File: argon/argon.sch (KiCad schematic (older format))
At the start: 72 parts, among them J1 USB, J2 V3V3-GND, J3 V3V3-GND, J4 V3V3-GND, J5 V3V3-GND, U1 LMC555xM, U2 AMS1117-3.3, U3 93LCxxA, U4 LMC555xM, U5 FT2232HL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

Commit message: Argon PCB - part 2 + logo
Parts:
- C17, C6: value 1uF -> 100nF
- H1, H2, H3, H4: footprint (none) -> MountingHole:MountingHole_3.2mm_M3
- R15, R3: value 100K -> 1M
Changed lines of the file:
@@
 	3800 10400 3650 10400
 Wire Wire Line
-	5000 10400 5000 10550
+	5050 10400 5050 10550
 $Comp
 L power:GND #PWR012
 U 1 1 5FD2B388
-P 5000 10550
-F 0 "#PWR012" H 5000 10300 50  0001 C CNN
-F 1 "GND" H 5005 10377 50  0000 C CNN
-F 2 "" H 5000 10550 50  0001 C CNN
-F 3 "" H 5000 10550 50  0001 C CNN
-	1    5000 10550
+P 5050 10550
+F 0 "#PWR012" H 5050 10300 50  0001 C CNN
+F 1 "GND" H 5055 10377 50  0000 C CNN
+F 2 "" H 5050 10550 50  0001 C CNN
+F 3 "" H 5050 10550 50  0001 C CNN
+	1    5050 10550
 	1    0    0    -1
 $EndComp
@@
 P 4700 10400
 F 0 "C6" V 4750 10250 50  0000 C CNN
-F 1 "1uF" V 4650 10250 50  0000 C CNN
+F 1 "100nF" V 4650 10200 50  0000 C CNN
 F 2 "Capacitor_SMD:C_0603_1608Metric" H 4700 10400 50  0001 C CNN
 F 3 "~" H 4700 10400 50  0001 C CNN
@@
 	4300 10400 4100 10400
 Wire Wire Line
-	4850 10400 5000 10400
+	4850 10400 5050 10400
 Wire Wire Line
 	2750 9850 2300 9850
@@
 P 3950 10400
 F 0 "R3" V 4050 10400 50  0000 C CNN
-F 1 "100K" V 3850 10400 50  0000 C CNN
+F 1 "1M" V 3850 10400 50  0000 C CNN
 F 2 "Resistor_SMD:R_0603_1608Metric" V 3880 10400 50  0001 C CNN
 F 3 "~" H 3950 10400 50  0001 C CNN
@@
 	8000 10400 7850 10400
 Wire Wire Line
-	9200 10400 9200 10550
+	9250 10400 9250 10550
 $Comp
 L power:GND #PWR024
 U 1 1 60E50CB0
-P 9200 10550
-F 0 "#PWR024" H 9200 10300 50  0001 C CNN
-F 1 "GND" H 9205 10377 50  0000 C CNN
-F 2 "" H 9200 10550 50  0001 C CNN
-F 3 "" H 9200 10550 50  0001 C CNN
-	1    9200 10550
+P 9250 10550
+F 0 "#PWR024" H 9250 10300 50  0001 C CNN
+F 1 "GND" H 9255 10377 50  0000 C CNN
+F 2 "" H 9250 10550 50  0001 C CNN
+F 3 "" H 9250 10550 50  0001 C CNN
+	1    9250 10550
 	1    0    0    -1
 $EndComp
@@
 P 8900 10400
 F 0 "C17" V 8950 10250 50  0000 C CNN
-F 1 "1uF" V 8850 10250 50  0000 C CNN
+F 1 "100nF" V 8850 10200 50  0000 C CNN
 F 2 "Capacitor_SMD:C_0603_1608Metric" H 8900 10400 50  0001 C CNN
 F 3 "~" H 8900 10400 50  0001 C CNN
@@
 	8500 10400 8300 10400
 Wire Wire Line
-	9050 10400 9200 10400
+	9050 10400 9250 10400
 Wire Wire Line
 	6950 9850 6500 9850
@@
 P 8150 10400
 F 0 "R15" V 8250 10400 50  0000 C CNN
-F 1 "100K" V 8050 10400 50  0000 C CNN
+F 1 "1M" V 8050 10400 50  0000 C CNN
 F 2 "Resistor_SMD:R_0603_1608Metric" V 8080 10400 50  0001 C CNN
 F 3 "~" H 8150 10400 50  0001 C CNN
@@
 F 0 "H1" H 15150 8096 50  0000 L CNN
 F 1 "MountingHole" H 15150 8005 50  0000 L CNN
-F 2 "" H 15050 8050 50  0001 C CNN
+F 2 "MountingHole:MountingHole_3.2mm_M3" H 15050 8050 50  0001 C CNN
 F 3 "~" H 15050 8050 50  0001 C CNN
 	1    15050 8050
@@
 F 0 "H2" H 15150 8346 50  0000 L CNN
 F 1 "MountingHole" H 15150 8255 50  0000 L CNN
-F 2 "" H 15050 8300 50  0001 C CNN
+F 2 "MountingHole:MountingHole_3.2mm_M3" H 15050 8300 50  0001 C CNN
 F 3 "~" H 15050 8300 50  0001 C CNN
 	1    15050 8300
@@
 F 0 "H3" H 15150 8596 50  0000 L CNN
 F 1 "MountingHole" H 15150 8505 50  0000 L CNN
-F 2 "" H 15050 8550 50  0001 C CNN
+F 2 "MountingHole:MountingHole_3.2mm_M3" H 15050 8550 50  0001 C CNN
 F 3 "~" H 15050 8550 50  0001 C CNN
 	1    15050 8550
@@
 F 0 "H4" H 15150 8846 50  0000 L CNN
 F 1 "MountingHole" H 15150 8755 50  0000 L CNN
-F 2 "" H 15050 8800 50  0001 C CNN
+F 2 "MountingHole:MountingHole_3.2mm_M3" H 15050 8800 50  0001 C CNN
 F 3 "~" H 15050 8800 50  0001 C CNN
 	1    15050 8800

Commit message: Change some capacitors to tantals
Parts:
- C12, C13, C7: footprint Capacitor_SMD:C_0603_1608Metric -> Capacitor_Tantalum_SMD:CP_EIA-3216-18_Kemet-A
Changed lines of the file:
@@
 F 0 "C7" H 5850 4500 50  0000 C CNN
 F 1 "4.7uF" H 5900 4300 50  0000 C CNN
-F 2 "Capacitor_SMD:C_0603_1608Metric" H 5750 4400 50  0001 C CNN
+F 2 "Capacitor_Tantalum_SMD:CP_EIA-3216-18_Kemet-A" H 5750 4400 50  0001 C CNN
 F 3 "~" H 5750 4400 50  0001 C CNN
 	1    5750 4400
@@
 F 0 "C12" H 7150 1650 50  0000 C CNN
 F 1 "4.7uF" H 7200 1450 50  0000 C CNN
-F 2 "Capacitor_SMD:C_0603_1608Metric" H 7050 1550 50  0001 C CNN
+F 2 "Capacitor_Tantalum_SMD:CP_EIA-3216-18_Kemet-A" H 7050 1550 50  0001 C CNN
 F 3 "~" H 7050 1550 50  0001 C CNN
 	1    7050 1550
@@
 F 0 "C13" H 7150 2650 50  0000 C CNN
 F 1 "4.7uF" H 7200 2450 50  0000 C CNN
-F 2 "Capacitor_SMD:C_0603_1608Metric" H 7050 2550 50  0001 C CNN
+F 2 "Capacitor_Tantalum_SMD:CP_EIA-3216-18_Kemet-A" H 7050 2550 50  0001 C CNN
 F 3 "~" H 7050 2550 50  0001 C CNN
 	1    7050 2550

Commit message: PCB - chaotic
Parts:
- D1, D2, D3, D4, D5, D6, D7: footprint LED_SMD:LED_0805_2012Metric -> benzene:LED_0805_2012Metric
- U1, U4: footprint Package_SO:SOIC-8_3.9x4.9mm_P1.27mm -> Package_SO:VSSOP-8_3.0x3.0mm_P0.65mm
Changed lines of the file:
@@
 F 0 "D1" H 4650 9550 50  0000 C CNN
 F 1 "LED" H 4650 9750 50  0000 C CNN
-F 2 "LED_SMD:LED_0805_2012Metric" H 4650 9650 50  0001 C CNN
+F 2 "benzene:LED_0805_2012Metric" H 4650 9650 50  0001 C CNN
 F 3 "~" H 4650 9650 50  0001 C CNN
 	1    4650 9650
@@
 F 0 "U1" H 3550 10200 50  0000 C CNN
 F 1 "LMC555xM" H 3500 9500 50  0000 C CNN
-F 2 "Package_SO:SOIC-8_3.9x4.9mm_P1.27mm" H 4100 9450 50  0001 C CNN
+F 2 "Package_SO:VSSOP-8_3.0x3.0mm_P0.65mm" H 4100 9450 50  0001 C CNN
 F 3 "http://www.ti.com/lit/ds/symlink/lmc555.pdf" H 4100 9450 50  0001 C CNN
 	1    3250 9850
@@
 F 0 "D4" H 14350 1150 50  0000 C CNN
 F 1 "LED" H 14350 1400 50  0000 C CNN
-F 2 "LED_SMD:LED_0805_2012Metric" H 14350 1250 50  0001 C CNN
+F 2 "benzene:LED_0805_2012Metric" H 14350 1250 50  0001 C CNN
 F 3 "~" H 14350 1250 50  0001 C CNN
 	1    14350 1250
@@
 F 0 "D5" H 14350 1550 50  0000 C CNN
 F 1 "LED" H 14350 1800 50  0000 C CNN
-F 2 "LED_SMD:LED_0805_2012Metric" H 14350 1650 50  0001 C CNN
+F 2 "benzene:LED_0805_2012Metric" H 14350 1650 50  0001 C CNN
 F 3 "~" H 14350 1650 50  0001 C CNN
 	1    14350 1650
@@
 F 0 "D6" H 14350 1950 50  0000 C CNN
 F 1 "LED" H 14350 2200 50  0000 C CNN
-F 2 "LED_SMD:LED_0805_2012Metric" H 14350 2050 50  0001 C CNN
+F 2 "benzene:LED_0805_2012Metric" H 14350 2050 50  0001 C CNN
 F 3 "~" H 14350 2050 50  0001 C CNN
 	1    14350 2050
@@
 F 0 "D7" H 14350 2350 50  0000 C CNN
 F 1 "LED" H 14350 2600 50  0000 C CNN
-F 2 "LED_SMD:LED_0805_2012Metric" H 14350 2450 50  0001 C CNN
+F 2 "benzene:LED_0805_2012Metric" H 14350 2450 50  0001 C CNN
 F 3 "~" H 14350 2450 50  0001 C CNN
 	1    14350 2450
@@
 F 0 "D3" H 8850 9550 50  0000 C CNN
 F 1 "LED" H 8850 9750 50  0000 C CNN
-F 2 "LED_SMD:LED_0805_2012Metric" H 8850 9650 50  0001 C CNN
+F 2 "benzene:LED_0805_2012Metric" H 8850 9650 50  0001 C CNN
 F 3 "~" H 8850 9650 50  0001 C CNN
 	1    8850 9650
@@
 F 0 "U4" H 7750 10200 50  0000 C CNN
 F 1 "LMC555xM" H 7700 9500 50  0000 C CNN
-F 2 "Package_SO:SOIC-8_3.9x4.9mm_P1.27mm" H 8300 9450 50  0001 C CNN
+F 2 "Package_SO:VSSOP-8_3.0x3.0mm_P0.65mm" H 8300 9450 50  0001 C CNN
 F 3 "http://www.ti.com/lit/ds/symlink/lmc555.pdf" H 8300 9450 50  0001 C CNN
 	1    7450 9850
@@
 F 0 "D2" H 5950 3050 50  0000 C CNN
 F 1 "LED" H 5950 3300 50  0000 C CNN
-F 2 "LED_SMD:LED_0805_2012Metric" H 5950 3150 50  0001 C CNN
+F 2 "benzene:LED_0805_2012Metric" H 5950 3150 50  0001 C CNN
 F 3 "~" H 5950 3150 50  0001 C CNN
 	1    5950 3150

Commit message: Piotrek's review
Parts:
- removed C5: 22uF, Capacitor_SMD:C_0603_1608Metric, symbol Device:C
- added C25, C5: 22uF, Capacitor_Tantalum_SMD:CP_EIA-3216-18_Kemet-A, symbol Device:CP1
- added U6: USBLC6-2SC6, Package_TO_SOT_SMD:SOT-23-6, symbol Power_Protection:USBLC6-2SC6
- C17, C6: symbol Device:CP1 -> Device:C
- C3, C9: value 10uF -> 10nF
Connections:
- net GND: now also C25.2, C5.2, U6.2 (GND)
- net V3V3: now also C5.1
- net VBUS: now reaches C4.1, J1.1 (VBUS), U2.3 (VI)
- net VBUS: now also C25.1, U6.5 (VBUS)
- net at J1.2 (D-): now also U6.1 (I/O1); no longer R12.2
- net at J1.3 (D+): now also U6.3 (I/O2); no longer R13.2
- new net: R12.2, U6.6 (I/O1)
- new net: R13.2, U6.4 (I/O2)
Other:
- moved on the sheet: C1, C2, C4, J1, R2, U2

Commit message: Argon - all elements and start paths
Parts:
- added J6, J7: V3V3-GND, Connector_PinHeader_2.54mm:PinHeader_1x02_P2.54mm_Vertical, symbol ArgonComponents:V3V3-GND
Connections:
- net GND: now also J6.1 (GND), J7.1 (GND)
- net V3V3: now also J6.2 (V3V3), J7.2 (V3V3)
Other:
- moved on the sheet: J2, J3, J4, J5
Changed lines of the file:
@@
 L ArgonComponents:V3V3-GND J2
 U 1 1 5FE8C355
-P 11550 8000
-F 0 "J2" H 11467 7777 50  0000 C CNN
-F 1 "V3V3-GND" H 11550 7800 50  0001 C CNN
-F 2 "Connector_PinHeader_2.54mm:PinHeader_1x02_P2.54mm_Vertical" H 11550 8000 50  0001 C CNN
-F 3 "~" H 11550 8000 50  0001 C CNN
-	1    11550 8000
-	-1   0    0    1
-$EndComp
-Wire Wire Line
-	11850 8000 12050 8000
-Wire Wire Line
-	12050 8000 12050 8100
-Wire Wire Line
-	11850 7900 12050 7900
+P 11550 7700
+F 0 "J2" H 11467 7477 50  0000 C CNN
+F 1 "V3V3-GND" H 11550 7500 50  0001 C CNN
+F 2 "Connector_PinHeader_2.54mm:PinHeader_1x02_P2.54mm_Vertical" H 11550 7700 50  0001 C CNN
+F 3 "~" H 11550 7700 50  0001 C CNN
+	1    11550 7700
+	-1   0    0    1
+$EndComp
+Wire Wire Line
+	11850 7700 12050 7700
+Wire Wire Line
+	12050 7700 12050 7800
+Wire Wire Line
+	11850 7600 12050 7600
 $Comp
 L power:GND #PWR027
 U 1 1 5FEAE107
-P 12050 8100
-F 0 "#PWR027" H 12050 7850 50  0001 C CNN
-F 1 "GND" H 12055 7927 50  0000 C CNN
-F 2 "" H 12050 8100 50  0001 C CNN
-F 3 "" H 12050 8100 50  0001 C CNN
-	1    12050 8100
-	1    0    0    -1
-$EndComp
-Text GLabel 12050 7900 2    50   Input ~ 0
+P 12050 7800
+F 0 "#PWR027" H 12050 7550 50  0001 C CNN
+F 1 "GND" H 12055 7627 50  0000 C CNN
+F 2 "" H 12050 7800 50  0001 C CNN
+F 3 "" H 12050 7800 50  0001 C CNN
+	1    12050 7800
+	1    0    0    -1
+$EndComp
+Text GLabel 12050 7600 2    50   Input ~ 0
 V3V3
 NoConn ~ 9750 7300
@@
 L ArgonComponents:V3V3-GND J3
 U 1 1 610EB3FD
-P 11550 8800
-F 0 "J3" H 11467 8577 50  0000 C CNN
-F 1 "V3V3-GND" H 11550 8600 50  0001 C CNN
-F 2 "Connector_PinHeader_2.54mm:PinHeader_1x02_P2.54mm_Vertical" H 11550 8800 50  0001 C CNN
-F 3 "~" H 11550 8800 50  0001 C CNN
-	1    11550 8800
-	-1   0    0    1
-$EndComp
-Wire Wire Line
-	11850 8800 12050 8800
-Wire Wire Line
-	12050 8800 12050 8900
-Wire Wire Line
-	11850 8700 12050 8700
+P 11550 8500
+F 0 "J3" H 11467 8277 50  0000 C CNN
+F 1 "V3V3-GND" H 11550 8300 50  0001 C CNN
+F 2 "Connector_PinHeader_2.54mm:PinHeader_1x02_P2.54mm_Vertical" H 11550 8500 50  0001 C CNN
+F 3 "~" H 11550 8500 50  0001 C CNN
+	1    11550 8500
+	-1   0    0    1
+$EndComp
+Wire Wire Line
+	11850 8500 12050 8500
+Wire Wire Line
+	12050 8500 12050 8600
+Wire Wire Line
+	11850 8400 12050 8400
 $Comp
 L power:GND #PWR0101
 U 1 1 610EB406
-P 12050 8900
-F 0 "#PWR0101" H 12050 8650 50  0001 C CNN
-F 1 "GND" H 12055 8727 50  0000 C CNN
-F 2 "" H 12050 8900 50  0001 C CNN
-F 3 "" H 12050 8900 50  0001 C CNN
-	1    12050 8900
-	1    0    0    -1
-$EndComp
-Text GLabel 12050 8700 2    50   Input ~ 0
+P 12050 8600
+F 0 "#PWR0101" H 12050 8350 50  0001 C CNN
+F 1 "GND" H 12055 8427 50  0000 C CNN
+F 2 "" H 12050 8600 50  0001 C CNN
+F 3 "" H 12050 8600 50  0001 C CNN
+	1    12050 8600
+	1    0    0    -1
+$EndComp
+Text GLabel 12050 8400 2    50   Input ~ 0
 V3V3
 $Comp
@@
 L ArgonComponents:V3V3-GND J4
 U 1 1 61468AEA
-P 13050 8000
-F 0 "J4" H 12967 7777 50  0000 C CNN
-F 1 "V3V3-GND" H 13050 7800 50  0001 C CNN
-F 2 "Connector_PinHeader_2.54mm:PinHeader_1x02_P2.54mm_Vertical" H 13050 8000 50  0001 C CNN
-F 3 "~" H 13050 8000 50  0001 C CNN
-	1    13050 8000
-	-1   0    0    1
-$EndComp
-Wire Wire Line
-	13350 8000 13550 8000
-Wire Wire Line
-	13550 8000 13550 8100
-Wire Wire Line
-	13350 7900 13550 7900
+P 13050 7700
+F 0 "J4" H 12967 7477 50  0000 C CNN
+F 1 "V3V3-GND" H 13050 7500 50  0001 C CNN
+F 2 "Connector_PinHeader_2.54mm:PinHeader_1x02_P2.54mm_Vertical" H 13050 7700 50  0001 C CNN
+F 3 "~" H 13050 7700 50  0001 C CNN
+	1    13050 7700
+	-1   0    0    1
+$EndComp
+Wire Wire Line
+	13350 7700 13550 7700
+Wire Wire Line
+	13550 7700 13550 7800
+Wire Wire Line
+	13350 7600 13550 7600
 $Comp
 L power:GND #PWR0102
 U 1 1 61468AF3
-P 13550 8100
-F 0 "#PWR0102" H 13550 7850 50  0001 C CNN
-F 1 "GND" H 13555 7927 50  0000 C CNN
-F 2 "" H 13550 8100 50  0001 C CNN
-F 3 "" H 13550 8100 50  0001 C CNN
-	1    13550 8100
-	1    0    0    -1
-$EndComp
-Text GLabel 13550 7900 2    50   Input ~ 0
+P 13550 7800
+F 0 "#PWR0102" H 13550 7550 50  0001 C CNN
+F 1 "GND" H 13555 7627 50  0000 C CNN
+F 2 "" H 13550 7800 50  0001 C CNN
+F 3 "" H 13550 7800 50  0001 C CNN
+	1    13550 7800
+	1    0    0    -1
+$EndComp
+Text GLabel 13550 7600 2    50   Input ~ 0
 V3V3
 $Comp
 L ArgonComponents:V3V3-GND J5
 U 1 1 61468AFA
-P 13050 8800
-F 0 "J5" H 12967 8577 50  0000 C CNN
-F 1 "V3V3-GND" H 13050 8600 50  0001 C CNN
-F 2 "Connector_PinHeader_2.54mm:PinHeader_1x02_P2.54mm_Vertical" H 13050 8800 50  0001 C CNN
-F 3 "~" H 13050 8800 50  0001 C CNN
-	1    13050 8800
-	-1   0    0    1
-$EndComp
-Wire Wire Line
-	13350 8800 13550 8800
-Wire Wire Line
-	13550 8800 13550 8900
-Wire Wire Line
-	13350 8700 13550 8700
+P 13050 8500
+F 0 "J5" H 12967 8277 50  0000 C CNN
+F 1 "V3V3-GND" H 13050 8300 50  0001 C CNN
+F 2 "Connector_PinHeader_2.54mm:PinHeader_1x02_P2.54mm_Vertical" H 13050 8500 50  0001 C CNN
+F 3 "~" H 13050 8500 50  0001 C CNN
+	1    13050 8500
+	-1   0    0    1
+$EndComp
+Wire Wire Line
+	13350 8500 13550 8500
+Wire Wire Line
+	13550 8500 13550 8600
+Wire Wire Line
+	13350 8400 13550 8400
 $Comp
 L power:GND #PWR0103
 U 1 1 61468B03
-P 13550 8900
-F 0 "#PWR0103" H 13550 8650 50  0001 C CNN
-F 1 "GND" H 13555 8727 50  0000 C CNN
-F 2 "" H 13550 8900 50  0001 C CNN
-F 3 "" H 13550 8900 50  0001 C CNN
-	1    13550 8900
-	1    0    0    -1
-$EndComp
-Text GLabel 13550 8700 2    50   Input ~ 0
+P 13550 8600
+F 0 "#PWR0103" H 13550 8350 50  0001 C CNN
+F 1 "GND" H 13555 8427 50  0000 C CNN
+F 2 "" H 13550 8600 50  0001 C CNN
+F 3 "" H 13550 8600 50  0001 C CNN
+	1    13550 8600
+	1    0    0    -1
+$EndComp
+Text GLabel 13550 8400 2    50   Input ~ 0
 V3V3
 Wire Wire Line
@@
 	3700 5100 3700 5050
 $Comp
-L power:GND #PWR?
+L power:GND #PWR034
 U 1 1 6043DCCE
 P 3700 5100
-F 0 "#PWR?" H 3700 4850 50  0001 C CNN
+F 0 "#PWR034" H 3700 4850 50  0001 C CNN
 F 1 "GND" H 3705 4927 50  0000 C CNN
 F 2 "" H 3700 5100 50  0001 C CNN
@@
 	1    0    0    -1
 $EndComp
+$Comp
+L ArgonComponents:V3V3-GND J6
+U 1 1 5FE49C5E
+P 11550 9250
+F 0 "J6" H 11467 9027 50  0000 C CNN
+F 1 "V3V3-GND" H 11550 9050 50  0001 C CNN
+F 2 "Connector_PinHeader_2.54mm:PinHeader_1x02_P2.54mm_Vertical" H 11550 9250 50  0001 C CNN
+F 3 "~" H 11550 9250 50  0001 C CNN
+	1    11550 9250
+	-1   0    0    1
+$EndComp
+Wire Wire Line
+	11850 9250 12050 9250
+Wire Wire Line
+	12050 9250 12050 9350
+Wire Wire Line
+	11850 9150 12050 9150
+$Comp
+L power:GND #PWR035
+U 1 1 5FE49C67
+P 12050 9350
+F 0 "#PWR035" H 12050 9100 50  0001 C CNN
+F 1 "GND" H 12055 9177 50  0000 C CNN
+F 2 "" H 12050 9350 50  0001 C CNN
+F 3 "" H 12050 9350 50  0001 C CNN
+	1    12050 9350
+	1    0    0    -1
+$EndComp
+Text GLabel 12050 9150 2    50   Input ~ 0
+V3V3
+$Comp
+L ArgonComponents:V3V3-GND J7
+U 1 1 5FE49C6E
+P 13050 9250
+F 0 "J7" H 12967 9027 50  0000 C CNN
+F 1 "V3V3-GND" H 13050 9050 50  0001 C CNN
+F 2 "Connector_PinHeader_2.54mm:PinHeader_1x02_P2.54mm_Vertical" H 13050 9250 50  0001 C CNN
+F 3 "~" H 13050 9250 50  0001 C CNN
+	1    13050 9250
+	-1   0    0    1
+$EndComp
+Wire Wire Line
+	13350 9250 13550 9250
+Wire Wire Line
+	13550 9250 13550 9350
+Wire Wire Line
+	13350 9150 13550 9150
+$Comp
+L power:GND #PWR036
+U 1 1 5FE49C77
+P 13550 9350
+F 0 "#PWR036" H 13550 9100 50  0001 C CNN
+F 1 "GND" H 13555 9177 50  0000 C CNN
+F 2 "" H 13550 9350 50  0001 C CNN
+F 3 "" H 13550 9350 50  0001 C CNN
+	1    13550 9350
+	1    0    0    -1
+$EndComp
+Text GLabel 13550 9150 2    50   Input ~ 0
+V3V3
 $EndSCHEMATC

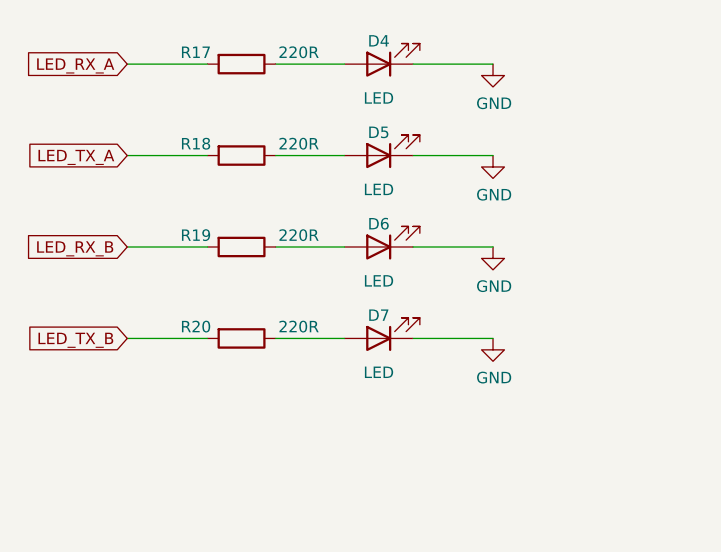
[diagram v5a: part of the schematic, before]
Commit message: Fix incorrectly designed LEDs
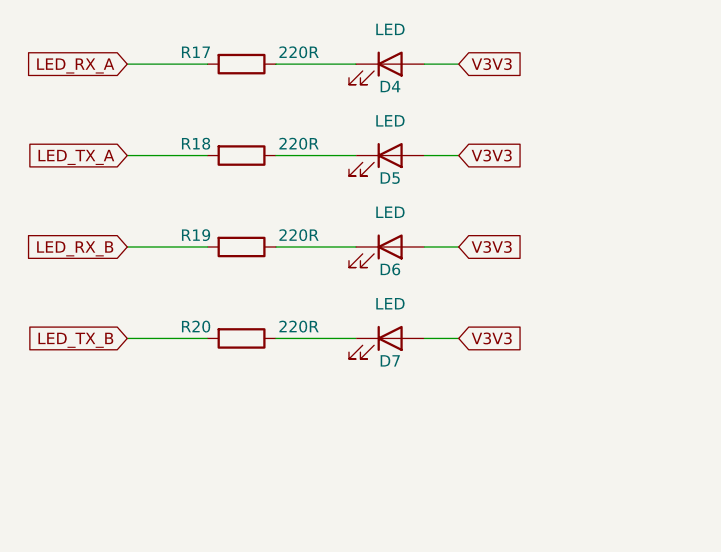
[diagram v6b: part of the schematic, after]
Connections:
- net GND: no longer D4.1 (K), D5.1 (K), D6.1 (K), D7.1 (K)
- net V3V3: now also D4.2 (A), D5.2 (A), D6.2 (A), D7.2 (A)
- net at R17.1: now also D4.1 (K); no longer D4.2 (A)
- net at R18.1: now also D5.1 (K); no longer D5.2 (A)
- net at R19.1: now also D6.1 (K); no longer D6.2 (A)
- net at R20.1: now also D7.1 (K); no longer D7.2 (A)
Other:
- moved on the sheet: D4, D5, D6, D7
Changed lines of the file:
@@
 L Device:LED D4
 U 1 1 604E42CC
-P 14350 1250
-F 0 "D4" H 14350 1150 50  0000 C CNN
-F 1 "LED" H 14350 1400 50  0000 C CNN
-F 2 "benzene:LED_0805_2012Metric" H 14350 1250 50  0001 C CNN
-F 3 "~" H 14350 1250 50  0001 C CNN
-	1    14350 1250
-	-1   0    0    1
+P 14400 1250
+F 0 "D4" H 14400 1150 50  0000 C CNN
+F 1 "LED" H 14400 1400 50  0000 C CNN
+F 2 "benzene:LED_0805_2012Metric" H 14400 1250 50  0001 C CNN
+F 3 "~" H 14400 1250 50  0001 C CNN
+	1    14400 1250
+	1    0    0    -1
 $EndComp
 $Comp
@@
 $EndComp
 Wire Wire Line
-	13900 1250 14200 1250
+	13900 1250 14250 1250
 Wire Wire Line
 	13600 1250 13250 1250
@@
 L Device:LED D5
 U 1 1 60BFE1C6
-P 14350 1650
-F 0 "D5" H 14350 1550 50  0000 C CNN
-F 1 "LED" H 14350 1800 50  0000 C CNN
-F 2 "benzene:LED_0805_2012Metric" H 14350 1650 50  0001 C CNN
-F 3 "~" H 14350 1650 50  0001 C CNN
-	1    14350 1650
-	-1   0    0    1
+P 14400 1650
+F 0 "D5" H 14400 1550 50  0000 C CNN
+F 1 "LED" H 14400 1800 50  0000 C CNN
+F 2 "benzene:LED_0805_2012Metric" H 14400 1650 50  0001 C CNN
+F 3 "~" H 14400 1650 50  0001 C CNN
+	1    14400 1650
+	1    0    0    -1
 $EndComp
 $Comp
@@
 $EndComp
 Wire Wire Line
-	13900 1650 14200 1650
+	13900 1650 14250 1650
 Wire Wire Line
 	13600 1650 13250 1650
@@
 L Device:LED D6
 U 1 1 60C0EA8F
-P 14350 2050
-F 0 "D6" H 14350 1950 50  0000 C CNN
-F 1 "LED" H 14350 2200 50  0000 C CNN
-F 2 "benzene:LED_0805_2012Metric" H 14350 2050 50  0001 C CNN
-F 3 "~" H 14350 2050 50  0001 C CNN
-	1    14350 2050
-	-1   0    0    1
+P 14400 2050
+F 0 "D6" H 14400 1950 50  0000 C CNN
+F 1 "LED" H 14400 2200 50  0000 C CNN
+F 2 "benzene:LED_0805_2012Metric" H 14400 2050 50  0001 C CNN
+F 3 "~" H 14400 2050 50  0001 C CNN
+	1    14400 2050
+	1    0    0    -1
 $EndComp
 $Comp
@@
 $EndComp
 Wire Wire Line
-	13900 2050 14200 2050
+	13900 2050 14250 2050
 Wire Wire Line
 	13600 2050 13250 2050
@@
 L Device:LED D7
 U 1 1 60C1F58D
-P 14350 2450
-F 0 "D7" H 14350 2350 50  0000 C CNN
-F 1 "LED" H 14350 2600 50  0000 C CNN
-F 2 "benzene:LED_0805_2012Metric" H 14350 2450 50  0001 C CNN
-F 3 "~" H 14350 2450 50  0001 C CNN
-	1    14350 2450
-	-1   0    0    1
+P 14400 2450
+F 0 "D7" H 14400 2350 50  0000 C CNN
+F 1 "LED" H 14400 2600 50  0000 C CNN
+F 2 "benzene:LED_0805_2012Metric" H 14400 2450 50  0001 C CNN
+F 3 "~" H 14400 2450 50  0001 C CNN
+	1    14400 2450
+	1    0    0    -1
 $EndComp
 $Comp
@@
 $EndComp
 Wire Wire Line
-	13900 2450 14200 2450
+	13900 2450 14250 2450
 Wire Wire Line
 	13600 2450 13250 2450
 Text GLabel 13250 2450 0    50   Input ~ 0
 LED_TX_B
-$Comp
-L power:GND #PWR028
-U 1 1 60C30C8D
-P 14850 1250
-F 0 "#PWR028" H 14850 1000 50  0001 C CNN
-F 1 "GND" H 14855 1077 50  0000 C CNN
-F 2 "" H 14850 1250 50  0001 C CNN
-F 3 "" H 14850 1250 50  0001 C CNN
-	1    14850 1250
-	1    0    0    -1
-$EndComp
-$Comp
-L power:GND #PWR029
-U 1 1 60C312F4
-P 14850 1650
-F 0 "#PWR029" H 14850 1400 50  0001 C CNN
-F 1 "GND" H 14855 1477 50  0000 C CNN
-F 2 "" H 14850 1650 50  0001 C CNN
-F 3 "" H 14850 1650 50  0001 C CNN
-	1    14850 1650
-	1    0    0    -1
-$EndComp
-$Comp
-L power:GND #PWR030
-U 1 1 60C314AF
-P 14850 2050
-F 0 "#PWR030" H 14850 1800 50  0001 C CNN
-F 1 "GND" H 14855 1877 50  0000 C CNN
-F 2 "" H 14850 2050 50  0001 C CNN
-F 3 "" H 14850 2050 50  0001 C CNN
-	1    14850 2050
-	1    0    0    -1
-$EndComp
-$Comp
-L power:GND #PWR031
-U 1 1 60C3169B
-P 14850 2450
-F 0 "#PWR031" H 14850 2200 50  0001 C CNN
-F 1 "GND" H 14855 2277 50  0000 C CNN
-F 2 "" H 14850 2450 50  0001 C CNN
-F 3 "" H 14850 2450 50  0001 C CNN
-	1    14850 2450
-	1    0    0    -1
-$EndComp
 Text GLabel 13250 2050 0    50   Input ~ 0
 LED_RX_B
 Wire Wire Line
-	14500 1250 14850 1250
-Wire Wire Line
-	14500 1650 14850 1650
-Wire Wire Line
-	14500 2050 14850 2050
-Wire Wire Line
-	14500 2450 14850 2450
+	14550 1250 14700 1250
+Wire Wire Line
+	14550 1650 14700 1650
+Wire Wire Line
+	14550 2050 14700 2050
+Wire Wire Line
+	14550 2450 14700 2450
 Text GLabel 1700 9650 0    50   Input ~ 0
 CS_A
@@
 Text GLabel 13550 9150 2    50   Input ~ 0
 V3V3
+Text GLabel 14700 1250 2    50   Input ~ 0
+V3V3
+Text GLabel 14700 1650 2    50   Input ~ 0
+V3V3
+Text GLabel 14700 2050 2    50   Input ~ 0
+V3V3
+Text GLabel 14700 2450 2    50   Input ~ 0
+V3V3
 $EndSCHEMATC
